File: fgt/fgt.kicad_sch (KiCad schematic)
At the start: 34 parts, among them J1 Conn_01x02, J2 USB_B_Mini, J4 Conn_01x06, SW1 Reset, SW2 SW-, SW3 SW_M/BOOT, SW4 SW+, U1 ESP32-C3-WROOM-02, U3 BMP280, U4 HT75xx-1-SOT89

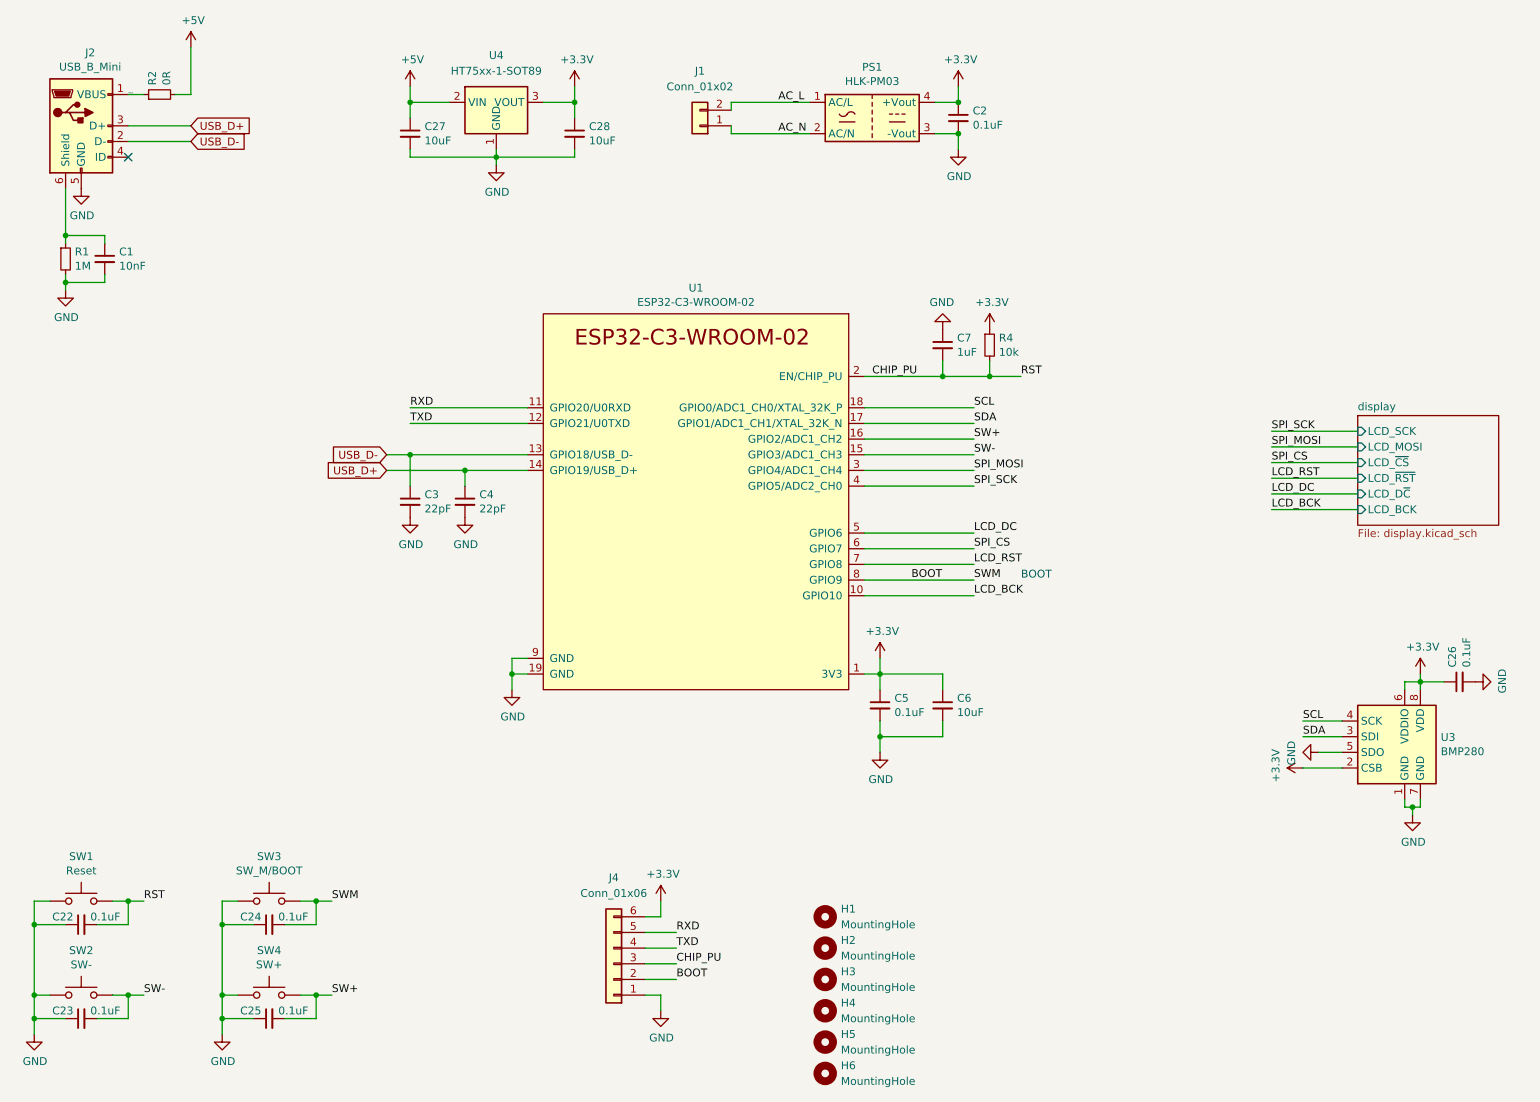
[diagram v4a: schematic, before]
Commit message: Release v1.4.0 - added testpoints - fix solder mask - size down pcb
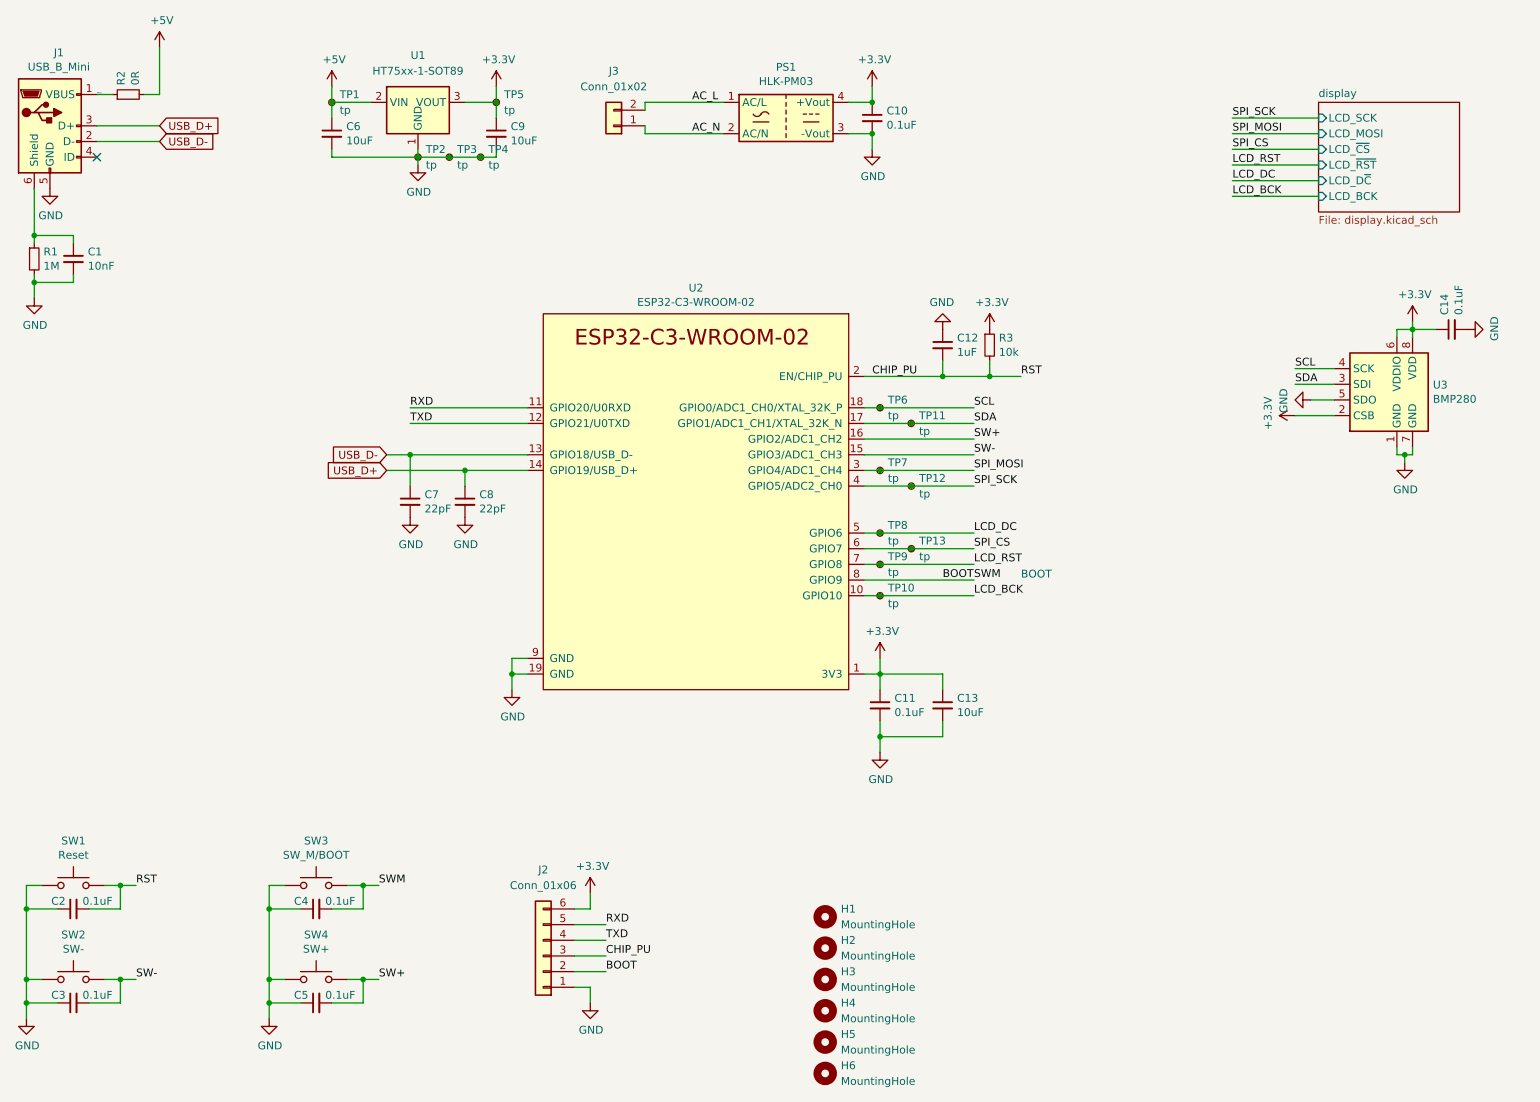
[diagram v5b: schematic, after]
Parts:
- added TP1, TP10, TP11, TP12, TP13, TP5, TP6, TP7, TP8, TP9: tp, TestPoint:TestPoint_Pad_D1.0mm, symbol Connector:TestPoint_Small
- added TP2, TP3, TP4: tp, TestPoint:TestPoint_Pad_1.0x1.0mm, symbol Connector:TestPoint_Small
- renumbered C2 to C10, C5 to C11, C7 to C12, C6 to C13, C26 to C14, C22 to C2, C23 to C3, C24 to C4, C25 to C5, C27 to C6, C3 to C7, C4 to C8, C28 to C9, J2 to J1, J4 to J2, J1 to J3, R4 to R3, U4 to U1, U1 to U2
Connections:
- net +3V3: now also TP5.1
- net +5V: now also TP1.1
- net GND: now also TP2.1, TP3.1, TP4.1
- net LCD_BCK: now also TP10.1
- net LCD_DC: now also TP8.1
- net LCD_RST: now also TP9.1
- net SCL: now also TP6.1
- net SDA: now also TP11.1
- net SPI_CS: now also TP13.1
- net SPI_MOSI: now also TP7.1
- net SPI_SCK: now also TP12.1
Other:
- moved on the sheet: C1, C10, C14, C2, C3, C4, C5, C6, C9, J1, J2, J3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

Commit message: Release v1.5.0 - See changelog for changes.
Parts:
- removed C10: 0.1uF, Capacitor_SMD:C_0805_2012Metric, symbol Device:C_Small
- removed C6, C9: 10uF, Capacitor_SMD:C_0805_2012Metric, symbol Device:C_Small
- removed C7, C8: 22pF, Capacitor_SMD:C_0603_1608Metric, symbol Device:C_Small
- removed J1: USB_B_Mini, Connector_USB:USB_Micro-B_Amphenol_10118194_Horizontal, symbol Connector:USB_B_Mini
- removed J3: Conn_01x02, Connector_Phoenix_MSTB:PhoenixContact_MSTBVA_2,5_2-G-5,08_1x02_P5.08mm_Vertical, symbol Connector_Generic:Conn_01x02
- removed PS1: HLK-PM03, Converter_ACDC:Converter_ACDC_HiLink_HLK-PMxx, symbol Converter_ACDC:HLK-PM03
- removed TP1, TP5: tp, TestPoint:TestPoint_Pad_D1.0mm, symbol Connector:TestPoint_Small
- removed TP2, TP3, TP4: tp, TestPoint:TestPoint_Pad_1.0x1.0mm, symbol Connector:TestPoint_Small
- removed U1: HT75xx-1-SOT89, Package_TO_SOT_SMD:SOT-89-3, symbol Regulator_Linear:HT75xx-1-SOT89
- added J5: MAIN, Connector_IDC:IDC-Header_2x03_P2.54mm_Vertical, symbol Connector_Generic:Conn_02x03_Odd_Even
- added JP1: SolderJumper_2_Bridged, Jumper:SolderJumper-2_P1.3mm_Bridged_RoundedPad1.0x1.5mm, symbol Jumper:SolderJumper_2_Bridged
- added Q2: IRLML6302, Package_TO_SOT_SMD:SOT-23, symbol Device:Q_PMOS_GSD
- added R11: 75k, Resistor_SMD:R_0805_2012Metric, symbol Device:R_Small
- R2: value 0R -> 240k
- renumbered TP6 to TP1, TP11 to TP2, TP7 to TP3, TP12 to TP4, TP8 to TP5, TP13 to TP6, TP9 to TP7, TP10 to TP8
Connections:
- net USB_D+ is gone; now on net SW+: U2.14 (GPIO19/USB_D+)
- net USB_D- is gone; now on net SW-: U2.13 (GPIO18/USB_D-)
- net +3V3: now also J5.1 (Pin_1), J5.6 (Pin_6)
- net BOOT: now also J2.5 (Pin_5); no longer J2.2 (Pin_2)
- net CHIP_PU: now also J2.4 (Pin_4); no longer J2.3 (Pin_3)
- net GND: now also J5.2 (Pin_2), J5.5 (Pin_5), R11.2; no longer R1.2
- net RXD: now also J2.3 (Pin_3); no longer J2.5 (Pin_5)
- net SW+: no longer U2.16 (GPIO2/ADC1_CH2)
- net SW-: no longer U2.15 (GPIO3/ADC1_CH3)
- net TXD: now also J2.2 (Pin_2); no longer J2.4 (Pin_4)
- net V_BAT: now reaches R1.1
- net V_BAT: now also Q2.2 (S); no longer C1.1
- net +5V renamed V_bat_adc
- net V_bat_adc: now also C1.1, U2.16 (GPIO2/ADC1_CH2), R11.1
- net LCD_BCK renamed B_CHECK
- net B_CHECK: now also R1.2, Q2.1 (G)
- net VBUS: no longer names the net of R2.1
- net VBUS: now also Q2.3 (D)
- new net DATA: J5.3 (Pin_3), J5.4 (Pin_4), U2.15 (GPIO3/ADC1_CH3)
- no-connect marks 1 -> 0
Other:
- added sheet Power (power.kicad_sch)
- note removed: "BOOT"
